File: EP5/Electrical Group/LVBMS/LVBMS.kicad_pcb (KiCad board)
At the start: 2 copper layers, 40 x 27.4 mm, 15 parts, among them J1 BAT, J2 OUT, Q1 TPCA8120,L1Q, U1 LM4041LP-ADJ, U2 LM2903

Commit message: update LVBMS for spaces
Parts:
- removed D1: 1N47xxA, Diode_SMD:D_MicroMELF_Handsoldering
- added R6: 2k5, Resistor_SMD:R_0805_2012Metric, F.Cu at (104.8, 72.6)
- added R7: 300k, Resistor_SMD:R_0805_2012Metric, F.Cu at (105.1, 65.4)
- J2: footprint Connector_JST:JST_VH_B2PS-VH_1x02_P3.96mm_Horizontal -> Connector_JST:JST_VH_B2P-VH-B_1x02_P3.96mm_Vertical
- R1: value 240R -> 13k
- R2: value 1k5 -> 82k
- R3: value 360k -> 300k
- RV1: value 330k -> 100k
- moved C2 3.93 mm to (99.4, 67.0)
- moved C1 3.07 mm to (83.3, 68.6)
- moved J1 2.96 mm to (75.8, 63.6)
- moved J2 2.01 mm to (77.5, 78.3)
- moved U1 1.68 mm to (99.3, 75.5)
- moved R1 1.12 mm to (102.4, 72.6)
- moved R2 0.72 mm to (103.1, 75.5), turned to 0 degrees
- moved RV1 0.25 mm to (107.2, 64.5)
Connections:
- RV1 pad 1: GNDPWR -> Net-(R7-Pad1)
- U1 pad 3: +24V -> GNDPWR
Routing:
- net Net-(R7-Pad1): track 0.00 -> 2.15 mm
- net Net-(U1-K): track 21.2 -> 20.4 mm
- net GNDPWR: track 4.82 -> 5.46 mm, vias 3 -> 4
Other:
- board size 40 x 27.4 mm -> 43.4 x 27.4 mm

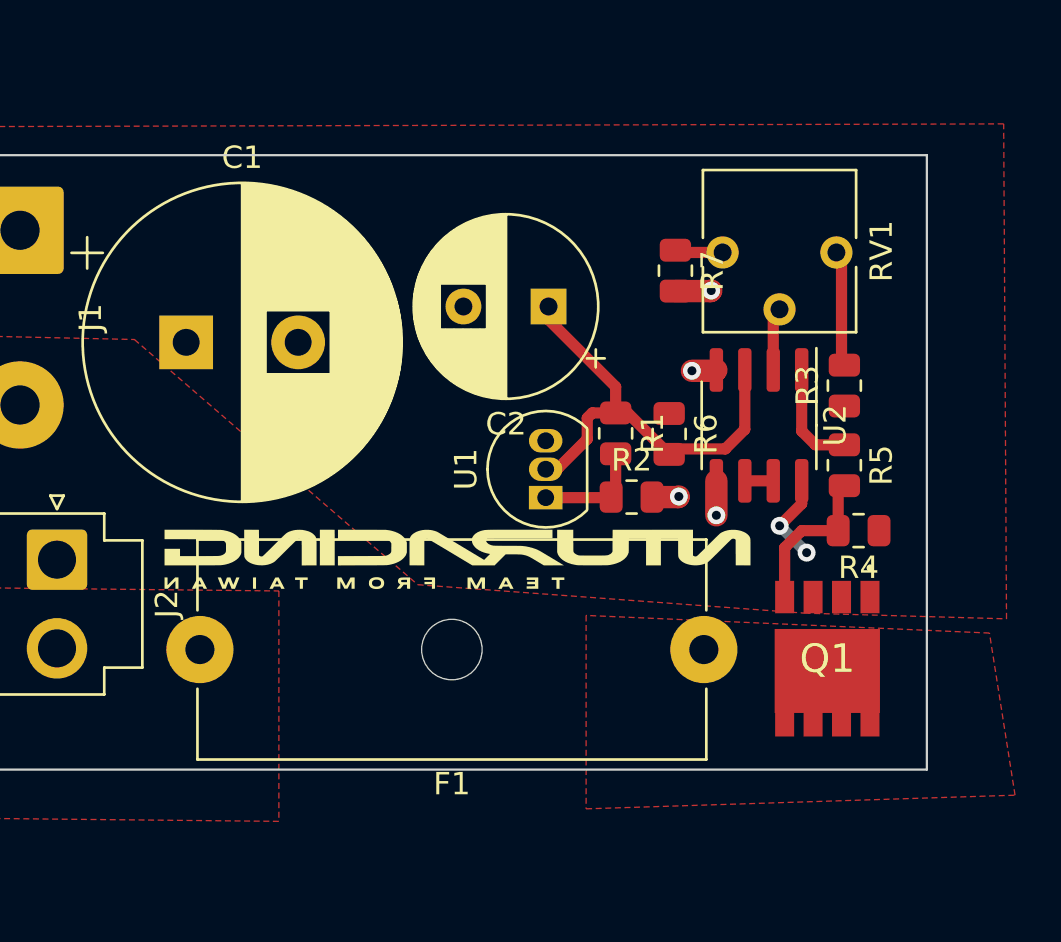
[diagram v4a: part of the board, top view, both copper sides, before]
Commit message: update LVBMS for better unused pin configuration
and better silkscreen layout
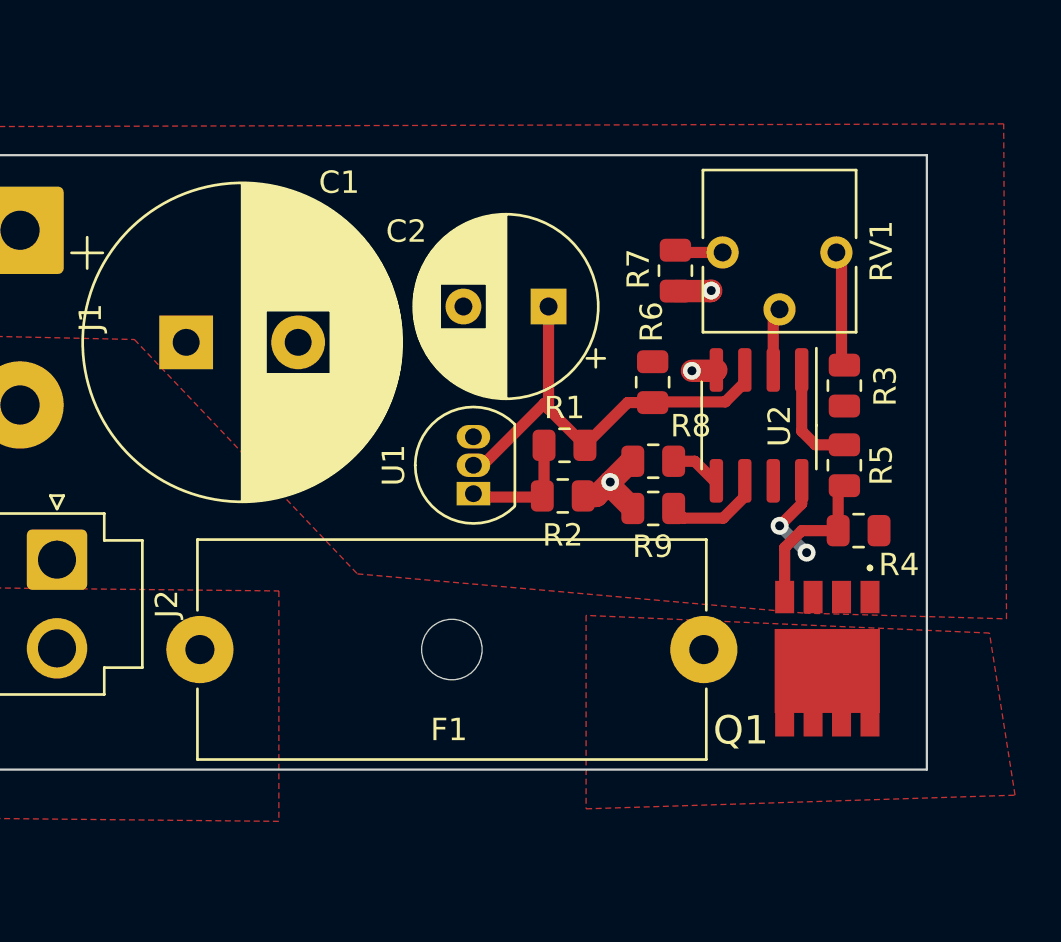
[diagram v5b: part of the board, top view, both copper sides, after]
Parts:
- added R8: 10k, Resistor_SMD:R_0805_2012Metric, F.Cu at (104.1, 73.9)
- added R9: 10M, Resistor_SMD:R_0805_2012Metric, F.Cu at (104.1, 76.0)
- moved U1 3.23 mm to (96.1, 75.3)
- moved R2 3.07 mm to (100.1, 75.4)
- moved R6 2.43 mm to (104.1, 70.3)
- moved R1 2.35 mm to (100.2, 73.2), turned to 180 degrees
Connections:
- U2 pad 5: GNDPWR -> Net-(U2B-+)
- U2 pad 7: Net-(U2B--) -> unconnected-(U2-Pad7)
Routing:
- net Net-(U2B--): track 1.27 -> 4.46 mm
- net Net-(U2B-+): track 0.00 -> 2.27 mm
- net GNDPWR: track 5.46 -> 7.17 mm, vias 4 -> 3
- net Net-(U1-FB): track 4.95 -> 5.45 mm

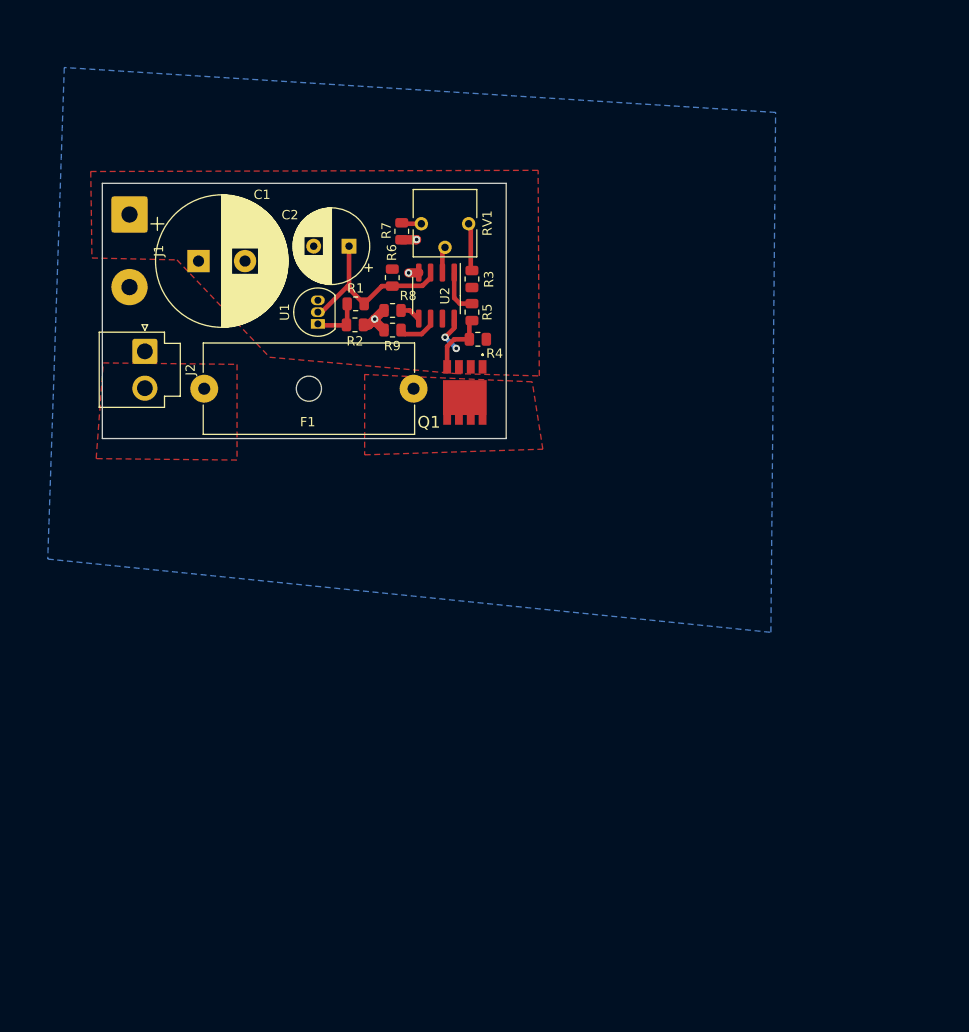
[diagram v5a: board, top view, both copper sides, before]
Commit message: update LVBMS to V2.0, more connectors
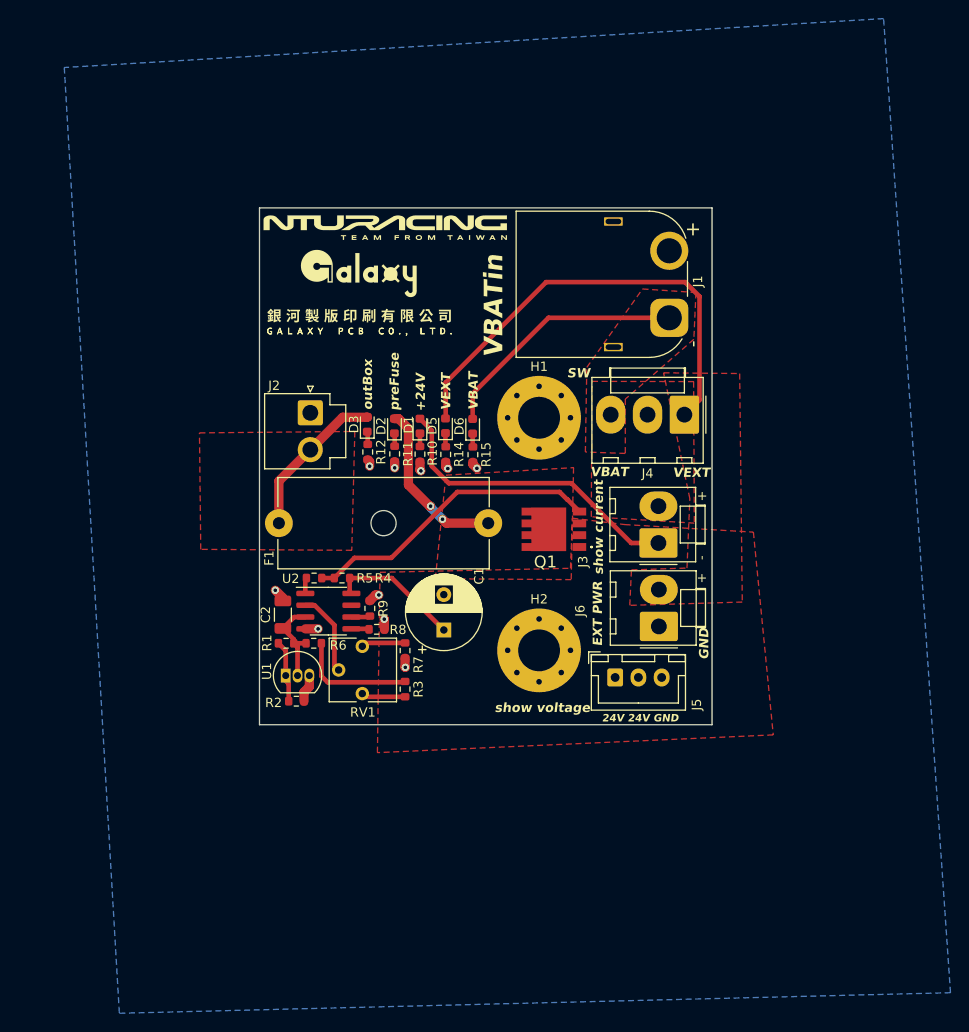
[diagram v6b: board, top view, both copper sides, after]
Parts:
- added D1: 24VGood, LED_SMD:LED_0603_1608Metric, F.Cu at (107.1, 86.3)
- added D2: 24Vprefuse, LED_SMD:LED_0603_1608Metric, F.Cu at (104.3, 86.3)
- added D3: 24Voutbox, LED_SMD:LED_0603_1608Metric, F.Cu at (101.4, 86.1)
- added D5: 24Vext, LED_SMD:LED_0603_1608Metric, F.Cu at (109.8, 86.3)
- added D6: 24Vbat, LED_SMD:LED_0603_1608Metric, F.Cu at (112.7, 86.3)
- added H1: MountingHole_Pad, MountingHole:MountingHole_4.5mm_Pad_Via, F.Cu at (119.9, 85.4)
- added H2: MountingHole_Pad, MountingHole:MountingHole_4.5mm_Pad_Via, F.Cu at (119.9, 110.4)
- added J3: showCurrent, Connector_Molex:Molex_KK-396_A-41791-0002_1x02_P3.96mm_Vertical, F.Cu at (132.7, 98.9)
- added J4: switch, Connector_Molex:Molex_KK-396_A-41791-0003_1x03_P3.96mm_Vertical, F.Cu at (135.5, 85.1)
- added J5: showVoltage, Connector_JST:JST_XH_B3B-XH-A_1x03_P2.50mm_Vertical, F.Cu at (128.0, 113.3)
- added J6: extPWR, Connector_Molex:Molex_KK-396_A-41791-0002_1x02_P3.96mm_Vertical, F.Cu at (132.7, 107.8)
- added R10: 5k, Resistor_SMD:R_0603_1608Metric, F.Cu at (107.1, 89.3)
- added R11: 5k, Resistor_SMD:R_0603_1608Metric, F.Cu at (104.3, 89.3)
- added R12: 5k, Resistor_SMD:R_0603_1608Metric, F.Cu at (101.4, 89.1)
- added R14: 5k, Resistor_SMD:R_0603_1608Metric, F.Cu at (109.8, 89.3)
- added R15: 5k, Resistor_SMD:R_0603_1608Metric, F.Cu at (112.8, 89.4)
- C1: value 1000u -> 100u; footprint Capacitor_THT:CP_Radial_D14.0mm_P5.00mm -> Capacitor_THT:CP_Radial_D8.0mm_P3.80mm
- C2: value 100u -> 22u 35V; footprint Capacitor_THT:CP_Radial_D8.0mm_P3.80mm -> Capacitor_SMD:C_1206_3216Metric
- J1: footprint Connector_Wire:SolderWire-1sqmm_1x02_P7.8mm_D1.4mm_OD3.9mm -> Connector_AMASS:AMASS_XT60PW-M_1x02_P7.20mm_Horizontal
- R1, R2, R3, R4, R5, R6, R7, R8, R9: footprint Resistor_SMD:R_0805_2012Metric -> Resistor_SMD:R_0603_1608Metric
- moved J1 59.1 mm to (133.9, 74.7), turned to 90 degrees
- moved C1 47.6 mm to (109.6, 108.2), turned to 90 degrees
- moved RV1 45.9 mm to (100.9, 110.0), turned to 180 degrees
- moved R7 45.1 mm to (105.5, 110.4)
- moved R3 44.7 mm to (105.5, 114.6), turned to -90 degrees
- moved R2 40.9 mm to (93.8, 115.9)
- moved C2 40.2 mm to (92.3, 106.6), turned to 90 degrees
- moved R6 40.2 mm to (95.6, 109.6), turned to 180 degrees
- moved U1 38.0 mm to (92.6, 113.1), turned to 0 degrees
- moved R1 37.2 mm to (92.7, 109.6)
- moved U2 35.9 mm to (97.2, 106.2), turned to 0 degrees
- moved R8 34.3 mm to (102.4, 108.1), turned to 180 degrees
- moved R5 33.2 mm to (95.7, 102.6), turned to 0 degrees
- moved R9 30.0 mm to (101.7, 105.9), turned to -90 degrees
- moved R4 29.5 mm to (98.7, 102.6)
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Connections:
- J1 pad 1: +24V -> /VBAT
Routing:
- net +24V: track 4.12 -> 60.4 mm, vias 2 -> 0
- net /VEXT: track 0.00 -> 49.6 mm
- net /VBAT: track 0.00 -> 27.2 mm
- net Net-(Q1-G): track 7.03 -> 32.4 mm
- net /+24V_prefuse: track 0.00 -> 18.4 mm, vias 0 -> 2
- net /+24V_outbox: track 0.00 -> 16.9 mm
- net Net-(U1-K): track 20.2 -> 9.96 mm
- net Net-(U2A--): track 2.82 -> 9.02 mm
- net GNDPWR: track 7.17 -> 13.2 mm, vias 3 -> 10
- net Net-(R5-Pad1): track 4.89 -> 1.70 mm
- net Net-(R7-Pad1): track 2.15 -> 4.75 mm
- net Net-(U2B--): track 4.46 -> 2.03 mm
- net Net-(D6-K): track 0.00 -> 1.50 mm
- net Net-(D5-K): track 0.00 -> 1.47 mm
- net Net-(D1-K): track 0.00 -> 1.41 mm
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- added copper zone on F.Cu, net /VBAT
- added copper zone on F.Cu, net /VEXT
- added copper zone on F.Cu, net /preShowCurrent
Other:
- board size 43.4 x 27.4 mm -> 48.6 x 55.5 mm
- board text added: "+"
- board text added: "+24V"
- board text added: "-"
- board text added: "24V 24V GND"
- board text added: "EP5 LVBMS V2.0 Jack Kuo"
- board text added: "EXT PWR"
- board text added: "GND"
- board text added: "SW"
- board text added: "VBAT"
- board text added: "VBATin"
- board text added: "VEXT"
- board text added: "outBox"
- board text added: "preFuse"
- board text added: "show current"
- board text added: "show voltage"

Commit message: update LVBMS to V2.1
fix XT60 reverse
fix show current should be at ground
fix lack of labeling
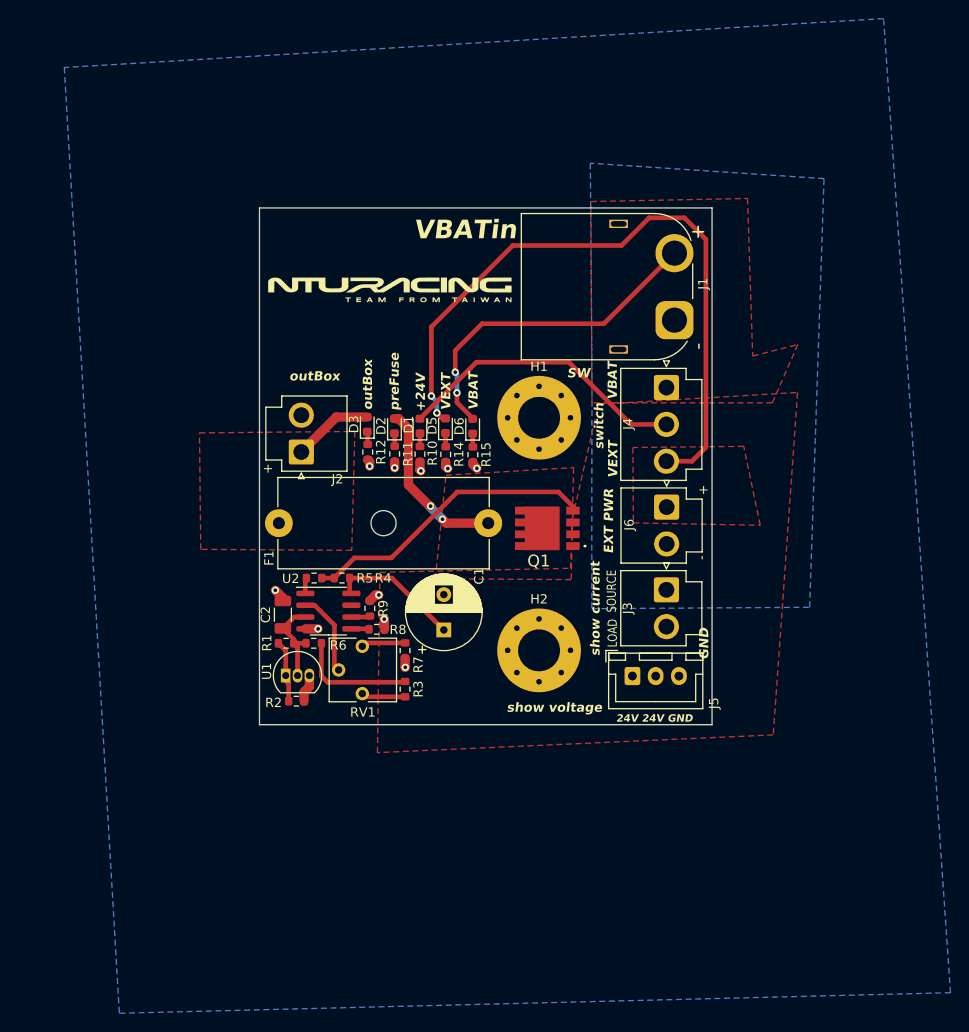
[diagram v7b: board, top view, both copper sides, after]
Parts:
- C1: value 100u -> 220u
- C2: value 22u 35V -> 10u 35V
- J3, J6: footprint Connector_Molex:Molex_KK-396_A-41791-0002_1x02_P3.96mm_Vertical -> Connector_JST:JST_VH_B2P-VH-B_1x02_P3.96mm_Vertical
- J4: footprint Connector_Molex:Molex_KK-396_A-41791-0003_1x03_P3.96mm_Vertical -> Connector_JST:JST_VH_B3P-VH_1x03_P3.96mm_Vertical
- R1: value 13k -> 12k
- R10, R11, R12, R14, R15: value 5k -> 10k
- R3, R7: value 300k -> 390k
- R4, R5: value 10k -> 100k
- R6: value 2k5 -> 10k
- moved J6 12.9 mm to (133.6, 95.0), turned to -90 degrees
- moved J3 5.10 mm to (133.6, 103.9), turned to -90 degrees
- moved J2 4.32 mm to (94.3, 89.1), turned to 90 degrees
- moved J4 3.50 mm to (133.6, 82.1), turned to -90 degrees
- moved J5 1.86 mm to (129.9, 113.2)
- moved Q1 0.71 mm to (120.8, 97.3)
- moved J1 0.61 mm to (134.4, 74.9)
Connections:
- J1 pad 1: /VBAT -> GND
- J1 pad 2: GNDPWR -> /VBAT
- J2 pad 1: GNDPWR -> /+24V_outbox
- J2 pad 2: /+24V_outbox -> GNDPWR
- J3 pad 1: +24V -> GND
- J3 pad 2: /preShowCurrent -> GNDPWR
- J4 pad 1: /VEXT -> /VBAT
- J4 pad 2: /preShowCurrent -> +24V
- J4 pad 3: /VBAT -> /VEXT
- J6 pad 1: GNDPWR -> /VEXT
- J6 pad 2: /VEXT -> GND
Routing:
- net /VEXT: track 49.6 -> 73.2 mm, vias 0 -> 2
- net /VBAT: track 27.2 -> 36.0 mm, vias 0 -> 2
- net /+24V_outbox: track 16.9 -> 8.64 mm
- net +24V: track 60.4 -> 58.8 mm
- added copper zone on B.Cu, net GND
- removed copper zone on F.Cu, net /preShowCurrent
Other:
- board text added: "EP5 LVBMS V2.1 Jack Kuo"
- board text added: "LOAD"
- board text added: "SOURCE"
- board text added: "switch"
- board text removed: "EP5 LVBMS V2.0 Jack Kuo"

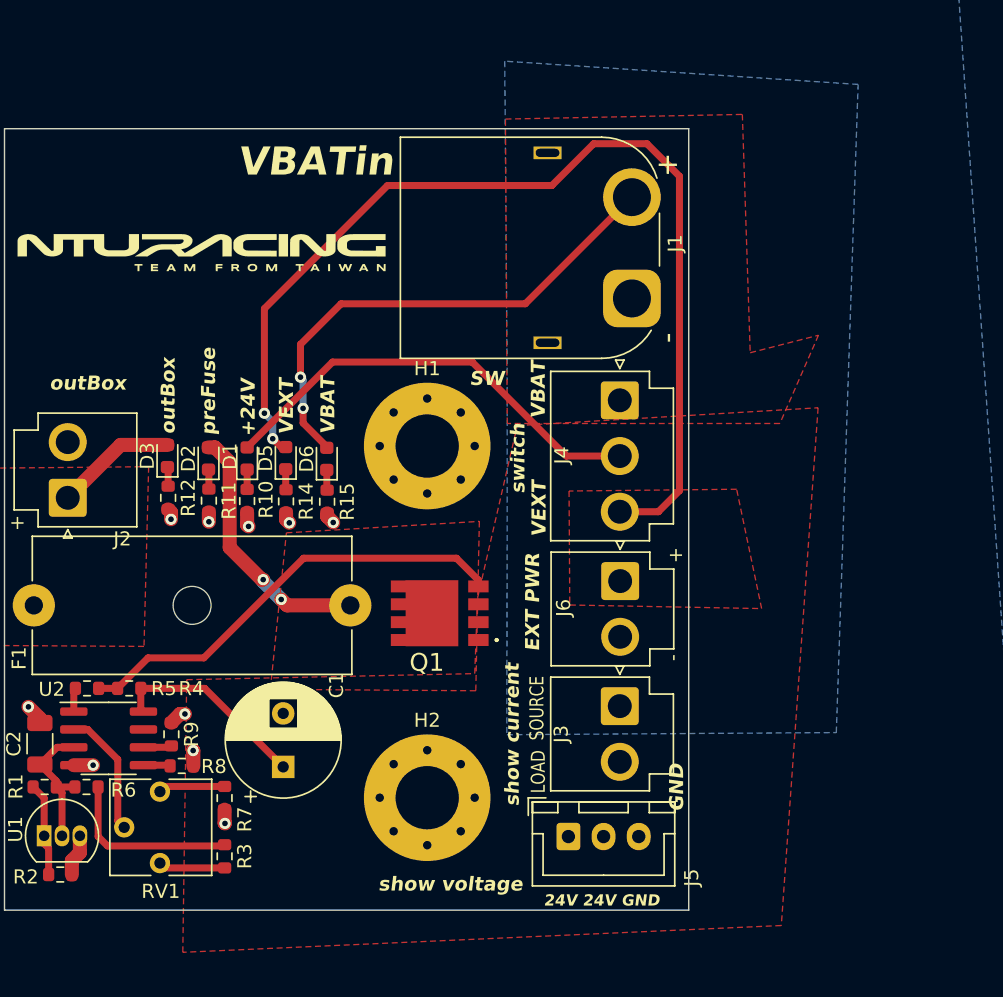
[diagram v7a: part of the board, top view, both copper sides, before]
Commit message: update LVBMS for kicad 8 and v 2.1
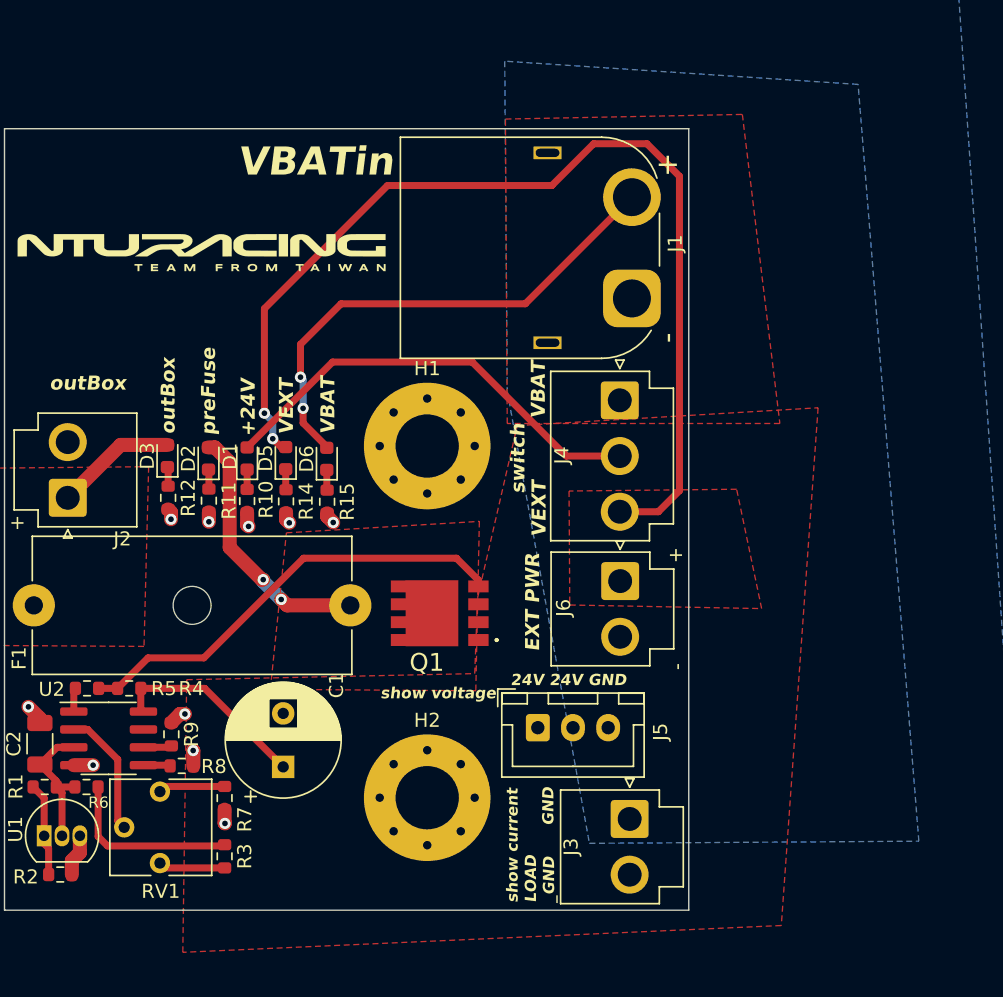
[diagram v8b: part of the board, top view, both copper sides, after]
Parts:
- moved J3 8.05 mm to (134.3, 111.9)
- moved J5 8.04 mm to (127.7, 105.4)
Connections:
- J5 pad 3: GNDPWR -> GND
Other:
- board text added: "LOAD _GND"
- board text added: "LOAD_GND"
- board text added: "current direction ==>"
- board text removed: "LOAD"
- board text removed: "SOURCE"
- board text removed: "SW"
